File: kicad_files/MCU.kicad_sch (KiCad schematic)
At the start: 25 parts, among them SW1 SW_Push, SW2 SW_Push, U1 STM32F407VGTx, Y1 LFXTAL036869Reel 8MHz Crystal

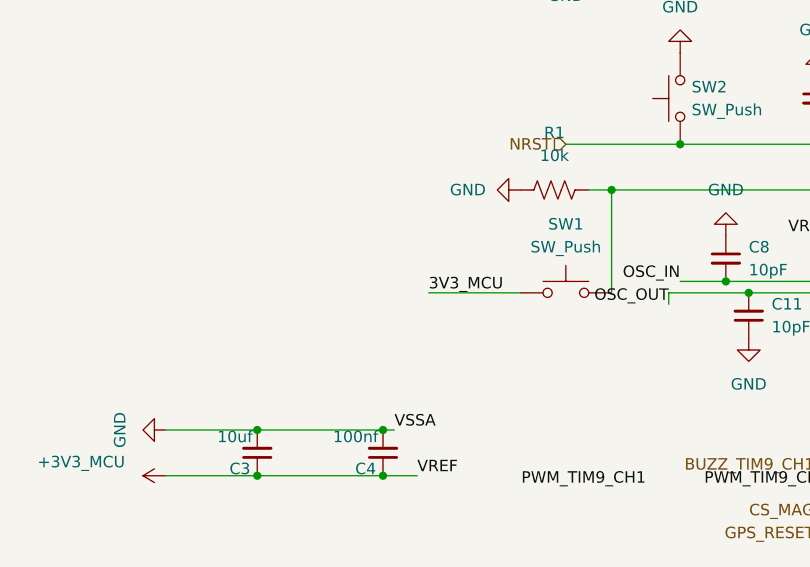
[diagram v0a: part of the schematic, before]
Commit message: Address all non-footprint DRC errors
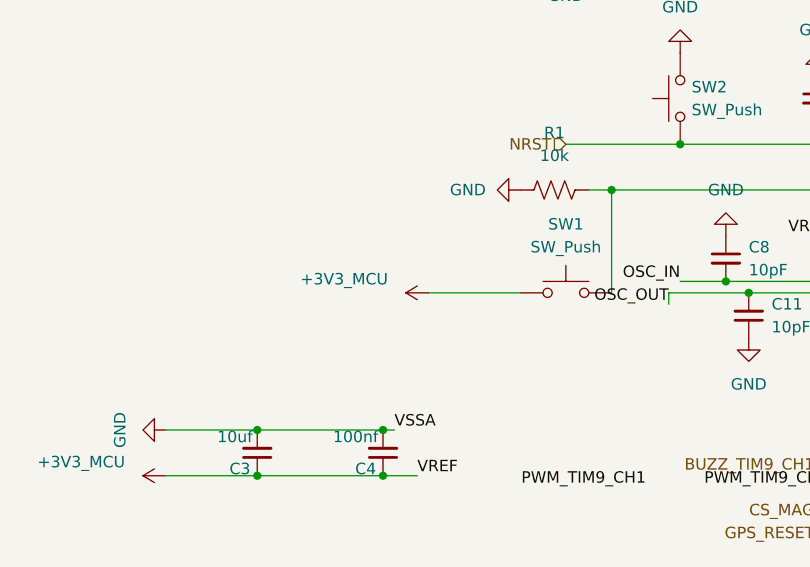
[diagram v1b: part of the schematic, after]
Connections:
- net 3V3_MCU is gone; now on net +3V3_MCU: SW1.1
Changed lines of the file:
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@@
-		)
-	)
-	(label "3V3_MCU"
-		(at 154.94 110.49 0)
-		(effects
-			(font
-				(size 1.27 1.27)
-			)
-			(justify left bottom)
 		)
 	)
@@
 					(unit 1)
 				)
+			)
+		)
+	)
+	(symbol
+		(lib_id "power:+3V0")
+		(at 154.94 110.49 90)
+		(unit 1)
+		(body_style 1)
+		(exclude_from_sim no)
+		(in_bom yes)
+		(on_board yes)
+		(in_pos_files yes)
+		(dnp no)
+		(property "Reference" "#PWR053"
+			(at 158.75 110.49 0)
+			(hide yes)
+			(show_name no)
+			(do_not_autoplace no)
+			(effects
+				(font
+					(size 1.27 1.27)
+				)
+			)
+		)
+		(property "Value" "+3V3_MCU"
+			(at 145.542 108.966 90)
+			(show_name no)
+			(do_not_autoplace no)
+			(effects
+				(font
+					(size 1.27 1.27)
+				)
+			)
+		)
+		(property "Footprint" ""
+			(at 154.94 110.49 0)
+			(hide yes)
+			(show_name no)
+			(do_not_autoplace no)
+			(effects
+				(font
+					(size 1.27 1.27)
+				)
+			)
+		)
+		(property "Datasheet" ""
+			(at 154.94 110.49 0)
+			(hide yes)
+			(show_name no)
+			(do_not_autoplace no)
+			(effects
+				(font
+					(size 1.27 1.27)
+				)
+			)
+		)
+		(property "Description" "Power symbol creates a global label with name \"+3V0\""
+			(at 154.94 110.49 0)
+			(hide yes)
+			(show_name no)
+			(do_not_autoplace no)
+			(effects
+				(font
+					(size 1.27 1.27)
+				)
+			)
+		)
+		(pin "1"
+		)
+		(instances
+			(project "versorlite"
+				(path "/1a230af0-0a74-48f7-8607-b087121dda49/a6e36be3-aff5-4566-a903-d81edfd88a96"
+					(reference "#PWR053")
+					(unit 1)
+				)

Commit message: fix unconnected
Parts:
- removed C3: 10uf, Capacitor_SMD:C_0805_2012Metric, symbol Device:C_Small
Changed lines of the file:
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@@
-	)
-	(junction
-		(at 135.89 130.81)
-		(diameter 0)
-		(color 0 0 0 0)
 	)
 	(junction
@@
 	)
 	(junction
-		(at 135.89 125.73)
-		(diameter 0)
-		(color 0 0 0 0)
-	)
-	(junction
 		(at 175.26 99.06)
 		(diameter 0)
@@
 	(wire
 		(pts
-			(xy 135.89 125.73) (xy 149.86 125.73)
-		)
-		(stroke
-			(width 0)
-			(type default)
-		)
-	)
-	(wire
-		(pts
 			(xy 217.17 80.01) (xy 219.71 80.01)
 		)
@@
 	(wire
 		(pts
-			(xy 125.73 125.73) (xy 135.89 125.73)
+			(xy 125.73 125.73) (xy 149.86 125.73)
 		)
 		(stroke
@@
 	(wire
 		(pts
-			(xy 135.89 130.81) (xy 149.86 130.81)
+			(xy 125.73 130.81) (xy 149.86 130.81)
 		)
 		(stroke
@@
 		(pts
 			(xy 175.26 99.06) (xy 175.26 110.49)
-		)
-		(stroke
-			(width 0)
-			(type default)
-		)
-	)
-	(wire
-		(pts
-			(xy 125.73 130.81) (xy 135.89 130.81)
 		)
 		(stroke
@@
 					(unit 1)
 				)
-			)
-		)
-	)
-	(symbol
-		(lib_id "Device:C_Small")
-		(at 135.89 128.27 180)
-		(unit 1)
-		(body_style 1)
-		(exclude_from_sim no)
-		(in_bom yes)
-		(on_board yes)
-		(in_pos_files yes)
-		(dnp no)
-		(property "Reference" "C3"
-			(at 135.128 130.048 0)
-			(show_name no)
-			(do_not_autoplace no)
-			(effects
-				(font
-					(size 1.27 1.27)
-				)
-				(justify left)
-			)
-		)
-		(property "Value" "10uf"
-			(at 135.382 126.492 0)
-			(show_name no)
-			(do_not_autoplace no)
-			(effects
-				(font
-					(size 1.27 1.27)
-				)
-				(justify left)
-			)
-		)
-		(property "Footprint" "Capacitor_SMD:C_0805_2012Metric"
-			(at 135.89 128.27 0)
-			(hide yes)
-			(show_name no)
-			(do_not_autoplace no)
-			(effects
-				(font
-					(size 1.27 1.27)
-				)
-			)
-		)
-		(property "Datasheet" ""
-			(at 135.89 128.27 0)
-			(hide yes)
-			(show_name no)
-			(do_not_autoplace no)
-			(effects
-				(font
-					(size 1.27 1.27)
-				)
-			)
-		)
-		(property "Description" "Unpolarized capacitor, small symbol"
-			(at 135.89 128.27 0)
-			(hide yes)
-			(show_name no)
-			(do_not_autoplace no)
-			(effects
-				(font
-					(size 1.27 1.27)
-				)
-			)
-		)
-		(pin "1"
-		)
-		(pin "2"
-		)
-		(instances
-			(project "versorlite"
-				(path "/1a230af0-0a74-48f7-8607-b087121dda49/a6e36be3-aff5-4566-a903-d81edfd88a96"
-					(reference "C3")
-					(unit 1)
-				)
